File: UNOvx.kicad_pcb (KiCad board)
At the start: 2 copper layers, 72 x 53.5 mm, 36 parts, among them IC1 BTS462T, J1 Barrel_Jack_Switch, J2 I2C/TWI, J3 Conn_01x02_Male, J4 Conn_02x03_Odd_Even, P1 Analog PC, P2 Power, P3 Digital PB, P4 Digital PD, P5 CONN_01X01, P6 CONN_01X01, P7 CONN_01X01, P8 CONN_01X01, SW1 SW_Push, U1 ATmega328P-PU, U2 NCP1117-5.0_SOT223, U3 LM358, Y1 16MHz, Y2 16MHz

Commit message: revA to rpod
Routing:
- net GND: vias 2 -> 3
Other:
- board text added: "rev.A"

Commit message: Rev. B
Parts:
- removed IC1: BTS462T, kicad-lib:TO-252-5PIN
- removed P8: CONN_01X01, Socket_Arduino_Uno:Arduino_1pin
- removed REF**: KiCad-Logo2_5mm_SilkScreen, Symbol:KiCad-Logo2_5mm_SilkScreen
- removed Y2: 16MHz, Crystal:Resonator_SMD_muRata_CDSCB-2Pin_4.5x2.0mm
- added D2: YellowTx, LED_SMD:LED_0805_2012Metric_Pad1.15x1.40mm_HandSolder, F.Cu at (173.7, 84.0)
- added D3: YellowRx, LED_SMD:LED_0805_2012Metric_Pad1.15x1.40mm_HandSolder, F.Cu at (176.3, 83.9)
- added D7: 1N4148W, Diode_SMD:D_SOD-123, F.Cu at (174.6, 94.8)
- added P5: Analog PC, Connector_PinHeader_2.54mm:PinHeader_1x06_P2.54mm_Vertical, F.Cu at (163.6, 120.3)
- added P7: CONN_01X01, Socket_Arduino_Uno:Arduino_1pin, F.Cu at (176.2, 99.4)
- added P7: Digital PD, Connector_PinHeader_2.54mm:PinHeader_1x08_P2.54mm_Vertical, F.Cu at (176.3, 79.1)
- added R3: 1k, Resistor_SMD:R_0805_2012Metric_Pad1.15x1.40mm_HandSolder, F.Cu at (176.3, 88.3)
- added R4: 1k, Resistor_SMD:R_0805_2012Metric_Pad1.15x1.40mm_HandSolder, F.Cu at (126.0, 90.8)
- C1, C2, C3, C5, C7: footprint Capacitor_SMD:C_0805_2012Metric -> Capacitor_SMD:C_0805_2012Metric_Pad1.15x1.40mm_HandSolder
- D4, D5: footprint LED_SMD:LED_0805_2012Metric -> LED_SMD:LED_0805_2012Metric_Pad1.15x1.40mm_HandSolder
- D6: value 1N4148W -> Yellow; footprint Diode_SMD:D_SOD-123 -> LED_SMD:LED_0805_2012Metric_Pad1.15x1.40mm_HandSolder
- J2: value I2C/TWI -> Conn_01x02; footprint Connector_PinHeader_2.54mm:PinHeader_1x02_P2.54mm_Vertical -> kicad-lib:MKDSN-2.5-1734656
- J3: value Conn_01x02_Male -> Conn_02x03_Odd_Even; footprint kicad-lib:MKDSN-2.5-1734656 -> Connector_PinHeader_2.54mm:PinHeader_2x03_P2.54mm_Vertical
- J4: value Conn_02x03_Odd_Even -> I2C/TWI; footprint Connector_PinHeader_2.54mm:PinHeader_2x03_P2.54mm_Vertical -> Connector_PinHeader_2.54mm:PinHeader_1x02_P2.54mm_Vertical
- P1: value Analog PC -> Power; footprint Socket_Arduino_Uno:Socket_Strip_Arduino_1x06 -> Connector_PinHeader_2.54mm:PinHeader_1x08_P2.54mm_Vertical
- P2: value Power -> Digital PB; footprint Connector_PinHeader_2.54mm:PinHeader_1x09_P2.54mm_Vertical -> Connector_PinHeader_2.54mm:PinHeader_1x06_P2.54mm_Vertical
- P3: footprint Socket_Arduino_Uno:Socket_Strip_Arduino_1x06 -> Connector_PinHeader_2.54mm:PinHeader_1x06_P2.54mm_Vertical
- P4: value Digital PD -> Analog PC; footprint Socket_Arduino_Uno:Socket_Strip_Arduino_1x08 -> Connector_PinHeader_2.54mm:PinHeader_1x06_P2.54mm_Vertical
- P6: value CONN_01X01 -> Digital PD; footprint Socket_Arduino_Uno:Arduino_1pin -> Connector_PinHeader_2.54mm:PinHeader_1x08_P2.54mm_Vertical
- R1: value 1M -> 1k; footprint Resistor_SMD:R_0805_2012Metric -> Resistor_SMD:R_0805_2012Metric_Pad1.15x1.40mm_HandSolder
- R2, R5: footprint Resistor_SMD:R_0805_2012Metric -> Resistor_SMD:R_0805_2012Metric_Pad1.15x1.40mm_HandSolder
- R6: value 1k -> 10k; footprint Resistor_SMD:R_0805_2012Metric -> Resistor_SMD:R_0805_2012Metric_Pad1.15x1.40mm_HandSolder
- R7: value 10k -> 330; footprint Resistor_SMD:R_0805_2012Metric -> Resistor_SMD:R_0805_2012Metric_Pad1.15x1.40mm_HandSolder
- Y1: footprint kicad-lib:CR23-crystal-11.3x4.5mm -> Crystal:Crystal_SMD_Abracon_ABM8G-4Pin_3.2x2.5mm
- moved J2 66.4 mm to (112.9, 88.3), turned to 90 degrees
- moved R2 60.3 mm to (173.7, 88.3)
- moved SW1 52.3 mm to (125.2, 76.8), turned to 0 degrees
- moved P2 50.8 mm to (153.4, 75.6), turned to 270 degrees
- moved P4 49.7 mm to (163.6, 123.8), turned to 90 degrees
- moved R6 47.3 mm to (175.1, 92.1), turned to 180 degrees
- moved J3 45.2 mm to (149.3, 114.3), turned to 270 degrees
- moved R7 44.6 mm to (135.4, 74.5), turned to 0 degrees
- moved D6 43.0 mm to (126.0, 81.9), turned to 180 degrees
- moved P6 39.4 mm to (176.3, 75.6), turned to 270 degrees
- moved J4 32.8 mm to (176.8, 104.8)
- moved D4 28.9 mm to (133.1, 115.7), turned to 0 degrees
- moved R1 27.5 mm to (133.1, 118.2), turned to 0 degrees
- moved P1 24.0 mm to (140.7, 123.8), turned to 90 degrees
- moved D1 22.9 mm to (114.1, 109.2), turned to 180 degrees
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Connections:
- D1 pad 2: Vin -> Net-(D1-Pad2)
- D6 pad 1: +5V -> GND
- D6 pad 2: Reset -> Net-(D6-Pad2)
- J1 pad 1: Vin -> Net-(D1-Pad2)
- J2 pad 1: A4(SDA) -> Net-(D1-Pad2)
- J2 pad 2: A5(SCL) -> GND
- J3 pad 1: Net-(IC1-Pad3) -> PB4(MISO)
- J3 pad 2: Net-(IC1-Pad5) -> +5V
- J4 pad 1: PB4(MISO) -> A4(SDA)
- J4 pad 2: +5V -> A5(SCL)
- P1 pad 1: A0 -> +5V
- P1 pad 2: A1 -> +5V
- P1 pad 3: A2 -> +5V
- P1 pad 4: A3 -> Reset
- P1 pad 5: A4(SDA) -> GND
- P1 pad 6: A5(SCL) -> GND
- P2 pad 1: Vin -> PB0(8)
- P2 pad 2: +5V -> PB1(9)
- P2 pad 3: +5V -> PB2(SS)
- P2 pad 4: +5V -> PB3(MOSI)
- P2 pad 5: Reset -> PB4(MISO)
- P2 pad 6: GND -> PB5(SCK)
- P4 pad 1: Rx -> A0
- P4 pad 2: Tx -> A1
- P4 pad 3: PD2 -> A2
- P4 pad 4: PD3 -> A3
- P4 pad 5: PD4 -> A4(SDA)
- P4 pad 6: PD5 -> A5(SCL)
- P5 pad 1: Net-(P5-Pad1) -> (no net)
- P6 pad 1: Net-(P6-Pad1) -> Rx
- P7 pad 1: Net-(P7-Pad1) -> (no net)
- R1 pad 1: XTAL1 -> +5V
- R1 pad 2: XTAL2 -> Net-(D4-Pad2)
- R2 pad 2: Net-(D4-Pad2) -> Net-(D2-Pad2)
- R5 pad 1: +5V -> Net-(R5-Pad1)
- R5 pad 2: Net-(D4-Pad2) -> Net-(D6-Pad2)
- R6 pad 1: Net-(R6-Pad1) -> +5V
- R6 pad 2: Net-(D5-Pad2) -> Reset
- R7 pad 1: +5V -> Net-(R7-Pad1)
- SW1 pad 1: Reset -> Net-(R7-Pad1)
- U3 pad 1: Net-(R6-Pad1) -> Net-(R4-Pad1)
- U3 pad 2: Net-(R6-Pad1) -> Net-(R4-Pad1)
- U3 pad 5: (no net) -> PB0(8)
- U3 pad 6: (no net) -> Net-(R5-Pad1)
- U3 pad 7: (no net) -> Net-(R5-Pad1)
- Y1 pad 2: XTAL1 -> GND
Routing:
- net Reset: track 66.1 -> 133.9 mm, vias 1 -> 3
- net +5V: track 116.5 -> 162.0 mm, vias 2 -> 4
- net GND: track 51.0 -> 11.4 mm, vias 3 -> 4
- net Net-(D1-Pad2): track 0.00 -> 29.8 mm
- net PB0(8): track 35.3 -> 62.3 mm, vias 2 -> 1
- net Net-(IC1-Pad3): track 20.2 -> 0.00 mm
- net Vin: track 18.9 -> 0.00 mm
- net XTAL2: track 21.2 -> 7.37 mm
- net PB4(MISO): track 52.9 -> 66.0 mm
- net Net-(R7-Pad1): track 0.00 -> 12.9 mm
- net XTAL1: track 19.3 -> 7.51 mm
- net Net-(C4-Pad1): track 28.6 -> 18.1 mm, vias 2 -> 0
- net Net-(R5-Pad1): track 0.00 -> 8.46 mm
- net PB3(MOSI): track 61.7 -> 69.6 mm
- net Net-(R4-Pad1): track 0.00 -> 7.53 mm
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- removed copper zone on F.Cu, net Net-(IC1-Pad3)
- removed copper zone on F.Cu, net Net-(IC1-Pad5)
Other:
- board size 72 x 53.5 mm -> 72 x 54 mm
- net class Default: trace_width 0.25 -> 0.4; via_dia 0.6 -> 0.8; via_drill 0.4 -> 0.5
- net class Power: clearance 0.6 -> 1; via_drill 0.6 -> 0.5
- net class Signal: clearance 0.4 -> 0.3; trace_width 0.25 -> 0.4; via_dia 0.6 -> 0.8; via_drill 0.4 -> 0.5
- rule trace_min: 0.2 -> 0.4
- rule via_min_drill: 0.3 -> 0.5
- rule via_min_size: 0.4 -> 0.6
- board text added: "Rev.B"
- board text removed: "<"
- board text removed: ">"
- board text removed: "Vin"
- board text removed: "rev.A"

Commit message: Use proper cap values for crystal
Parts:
- C3, C5: value 22pF -> 30pF
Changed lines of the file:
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@@
       (effects (font (size 1 1) (thickness 0.15)))
     )
-    (fp_text value 22pF (at 0 1.65 135) (layer F.Fab)
+    (fp_text value 30pF (at 0 1.65 135) (layer F.Fab)
       (effects (font (size 1 1) (thickness 0.15)))
     )
@@
       (effects (font (size 1 1) (thickness 0.15)))
     )
-    (fp_text value 22pF (at 0 1.65 45) (layer F.Fab)
+    (fp_text value 30pF (at 0 1.65 45) (layer F.Fab)
       (effects (font (size 1 1) (thickness 0.15)))
     )

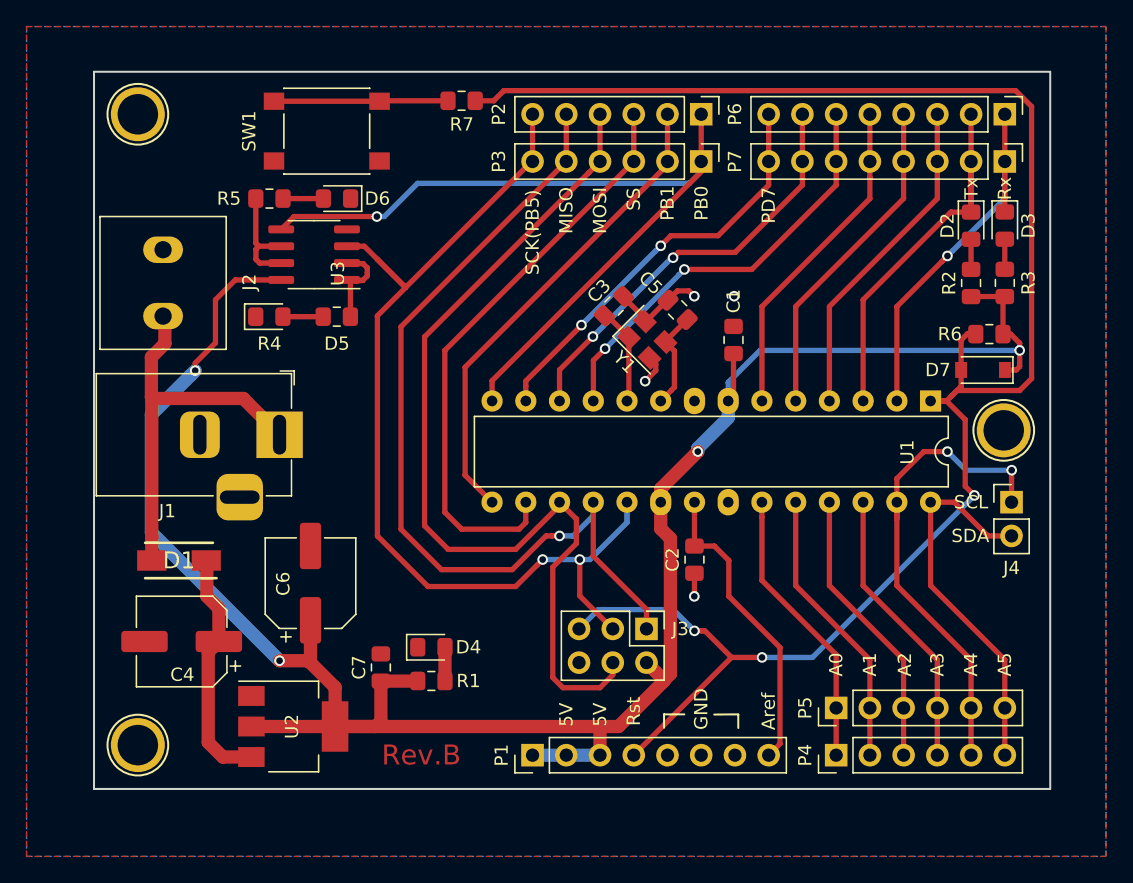
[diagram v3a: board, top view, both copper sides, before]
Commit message: Different crystal layout with own ground
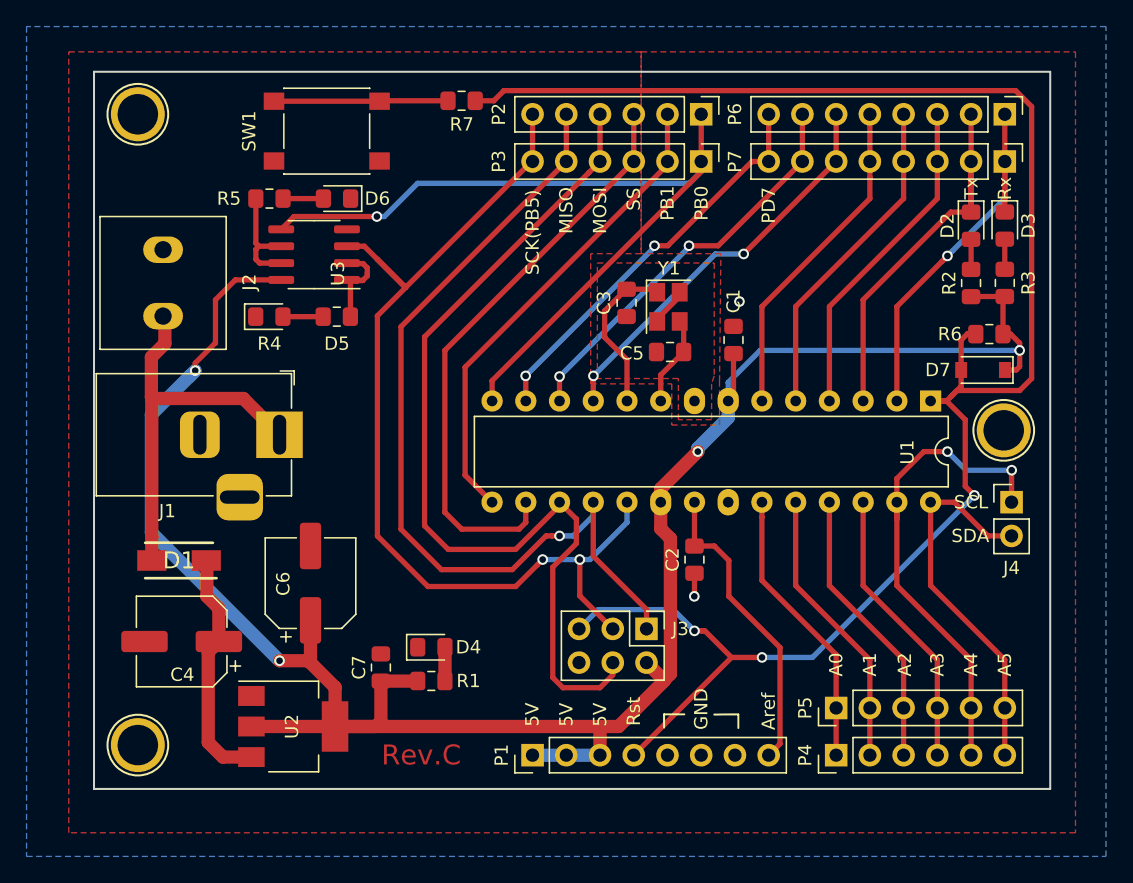
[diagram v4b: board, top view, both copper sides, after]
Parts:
- moved C5 3.22 mm to (151.1, 93.5), turned to 0 degrees
- moved Y1 2.94 mm to (150.9, 90.1), turned to 270 degrees
- moved C3 0.98 mm to (147.8, 89.8), turned to 90 degrees
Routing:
- net GND: track 11.4 -> 4.65 mm, vias 4 -> 2
- net XTAL2: track 7.37 -> 12.2 mm
- net PD5: track 32.1 -> 30.4 mm
- net PD6: track 31.7 -> 30.5 mm
- net PD7: track 31.2 -> 30.5 mm
- net XTAL1: track 7.51 -> 6.83 mm
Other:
- net class Default: clearance 0.3 -> 0.2
- rule trace_clearance: 0.3 -> 0.2
- board text added: "Rev.C"
- board text removed: "Rev.B"
